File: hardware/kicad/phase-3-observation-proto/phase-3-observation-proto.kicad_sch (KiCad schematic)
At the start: 34 parts, among them J1 Input_4pin, J2 Host_8pin, Q1 BC547, Q10 BC547, Q11 BC547, Q12 BC547, Q2 BC547, Q3 BC547, Q4 BC547, Q5 BC547, Q6 BC547, Q7 BC547, Q8 BC547, Q9 BC547, U1 74HC86

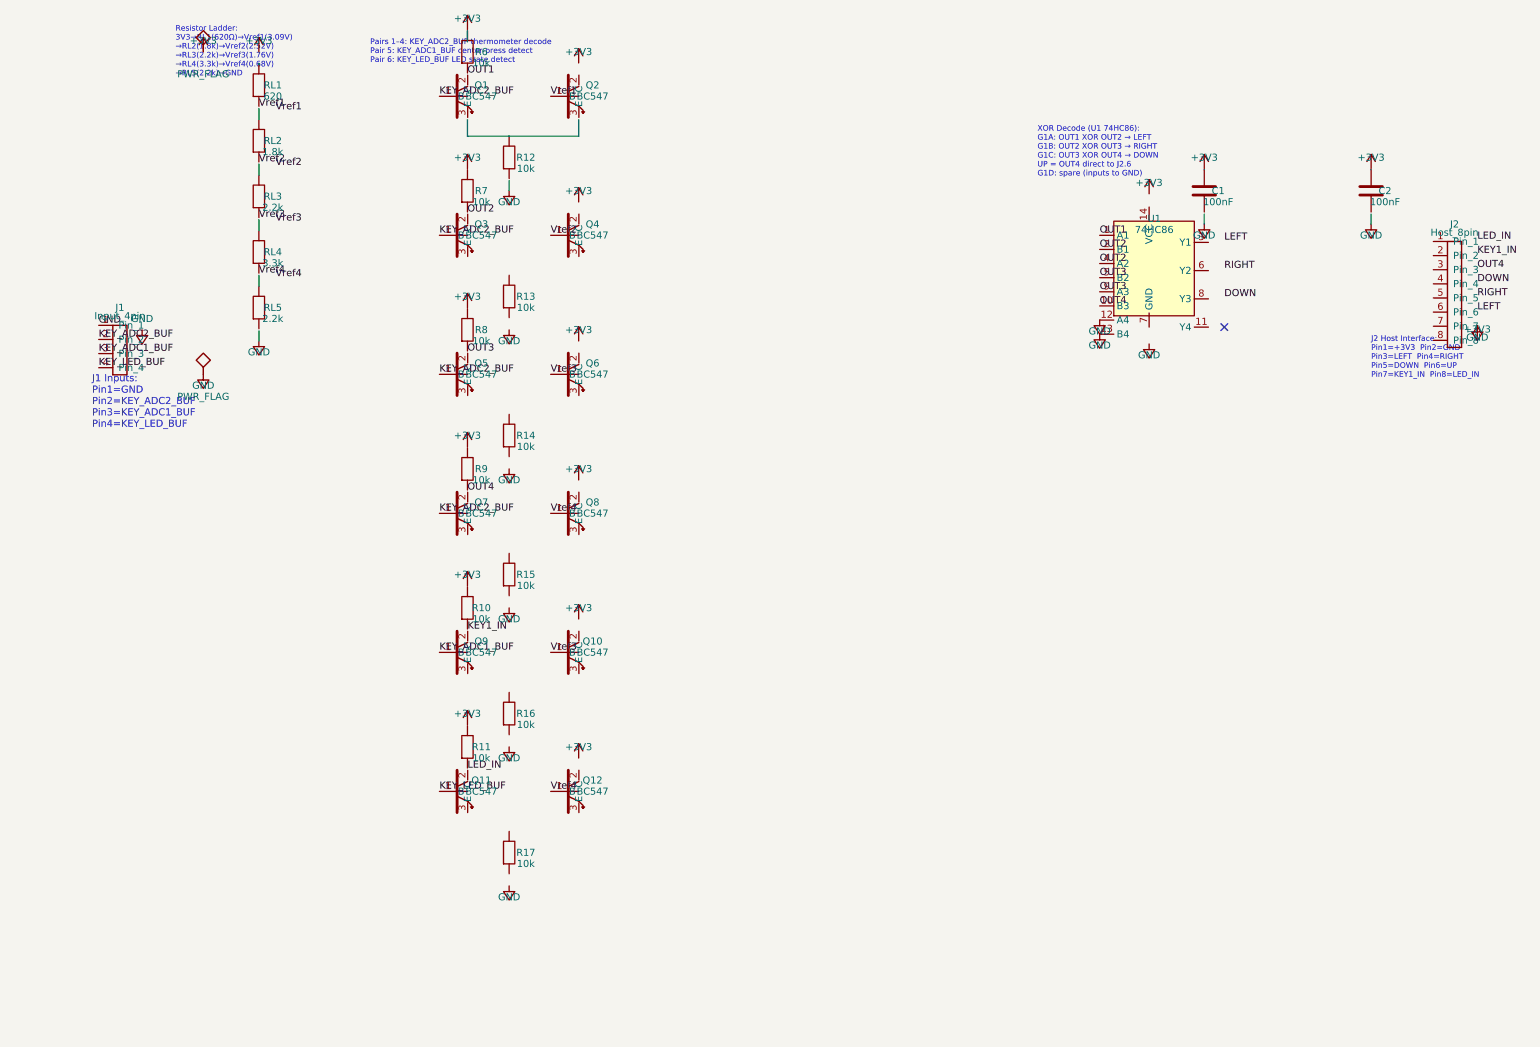
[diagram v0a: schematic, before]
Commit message: Protoboard design test
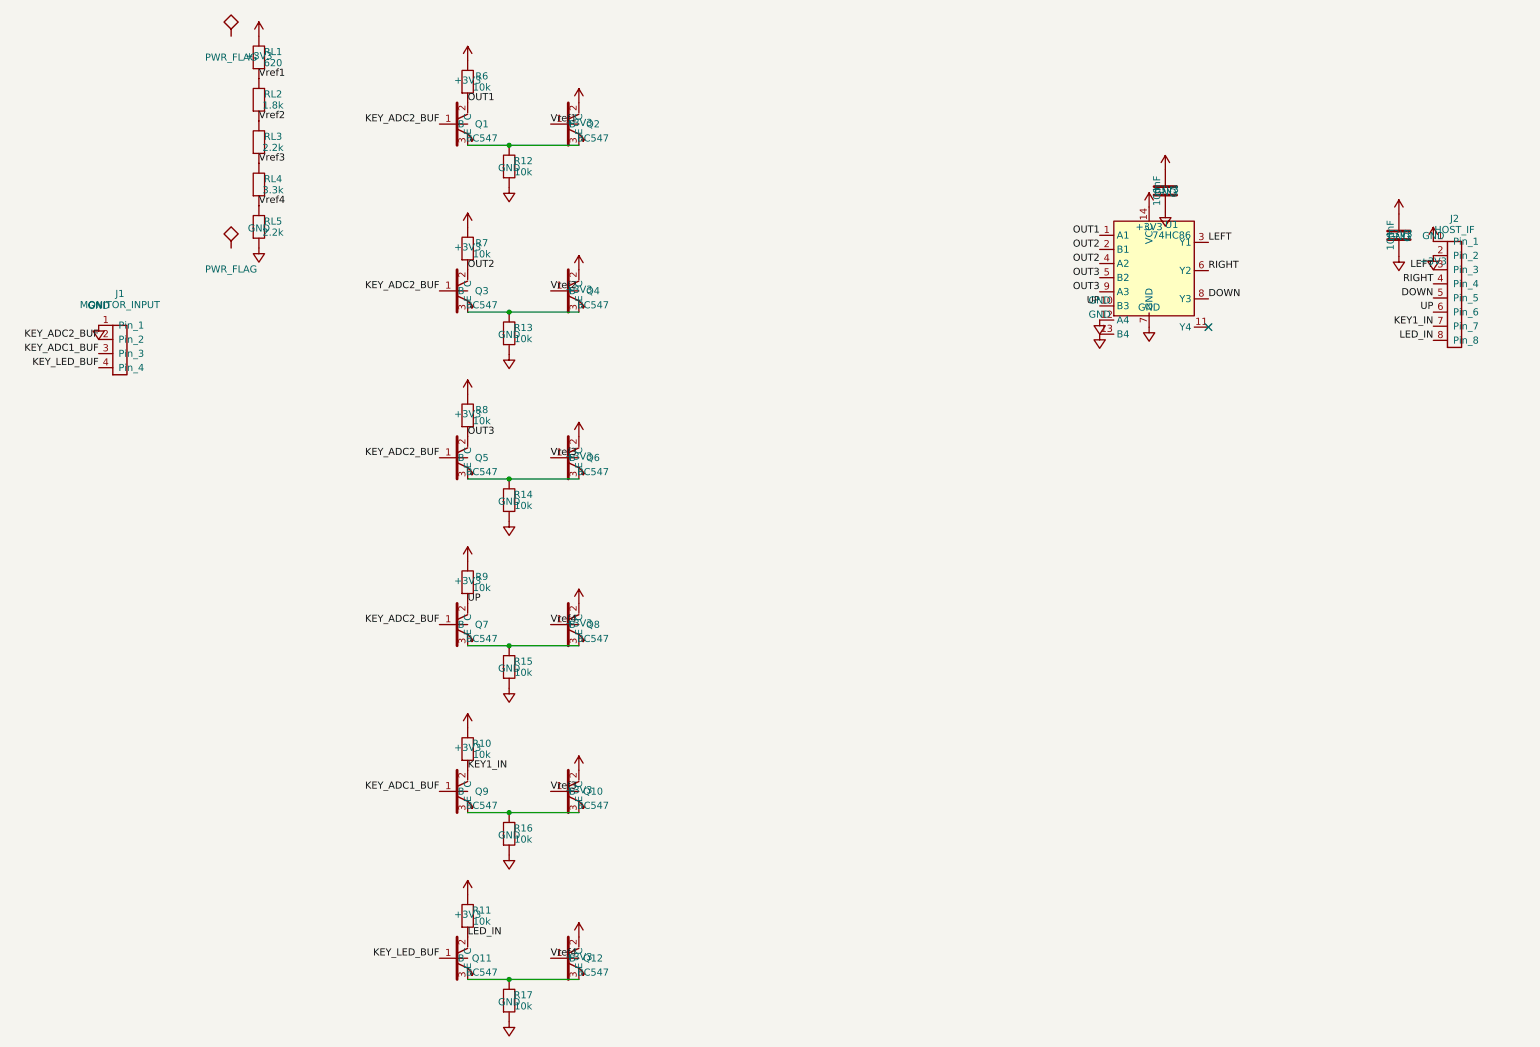
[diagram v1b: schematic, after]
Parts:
- J1: value Input_4pin -> MONITOR_INPUT
- J2: value Host_8pin -> HOST_IF
- Q1, Q10, Q11, Q12, Q2, Q3, Q4, Q5, Q6, Q7, Q8, Q9: footprint (none) -> Package_TO_SOT_THT:TO-92_Inline
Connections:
- net OUT4 is gone; now on net UP: U1.10 (B3)
- net DOWN: now also J2.5 (Pin_5)
- net KEY1_IN: now also J2.7 (Pin_7), Q9.2 (C), R10.2
- net LED_IN: now also J2.8 (Pin_8), Q11.2 (C), R11.2
- net LEFT: now also J2.3 (Pin_3)
- net OUT1: now also Q1.2 (C), R6.2
- net OUT2: now also Q3.2 (C), R7.2
- net OUT3: now also Q5.2 (C), R8.2
- net RIGHT: now also J2.4 (Pin_4)
- net Vref1: now also RL1.2
- net Vref2: now also RL2.2
- net Vref3: now also RL3.2
- net Vref4: now also RL4.2
- net at Q8.3 (E): now also Q7.3 (E), R15.1
- net at Q9.3 (E): now also Q10.3 (E), R16.1
- net at Q4.3 (E): now also Q3.3 (E), R13.1
- net at Q1.3 (E): now also Q2.3 (E), R12.1
- net at Q12.3 (E): now also Q11.3 (E), R17.1
- net at Q6.3 (E): now also Q5.3 (E), R14.1
- net UP: now reaches R9.2
- net UP: now also Q7.2 (C)
- net GND: no longer names the net of J1.1 (Pin_1)
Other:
- note removed: "J1 Inputs: Pin1=GND Pin2=KEY_ADC2_BUF Pin3=KEY_ADC1_BUF Pin4=KEY_LED_BUF"
- note removed: "J2 Host Interface: Pin1=+3V3 Pin2=GND Pin3=LEFT Pin4=RIGHT Pin5=DOWN Pin6=UP Pin7=KEY1_IN Pin8=LED_IN"
- note removed: "Pairs 1–4: KEY_ADC2_BUF thermometer decode Pair 5: KEY_ADC1_BUF center-press detect Pair 6: KEY_LED_BUF LED state detect"
- note removed: "Resistor Ladder: 3V3→RL1(620Ω)→Vref1(3.09V) →RL2(1.8k)→Vref2(2.52V) →RL3(2.2k)→Vref3(1.76V) →RL4(3.3k)→Vref4(0.68V) →RL5(2.2k)→GND"
- note removed: "XOR Decode (U1 74HC86): G1A: OUT1 XOR OUT2 → LEFT G1B: OUT2 XOR OUT3 → RIGHT G1C: OUT3 XOR OUT4 → DOWN UP = OUT4 direct to J2.6 G1D: spare (inputs to GND)"
